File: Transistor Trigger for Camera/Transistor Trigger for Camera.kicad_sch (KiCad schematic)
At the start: 10 parts, among them J1 Conn_01x01_Pin, J2 Conn_01x01_Pin, J3 Conn_01x01_Pin, J4 Conn_01x01_Pin, J5 Conn_01x01_Pin, J6 Conn_01x01_Pin, Q1 2N4401, U1 74HC14N_652

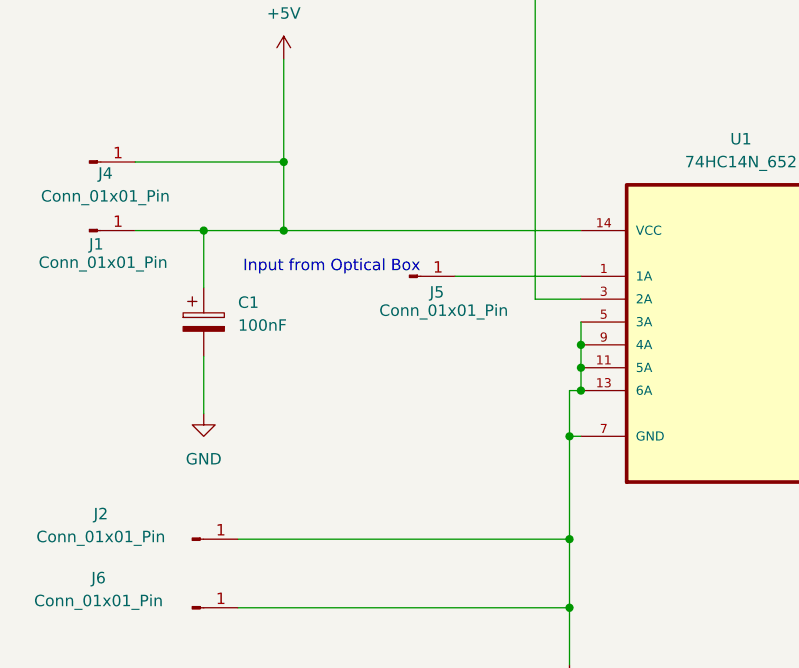
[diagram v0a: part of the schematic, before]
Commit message: second update with new 100k resistor
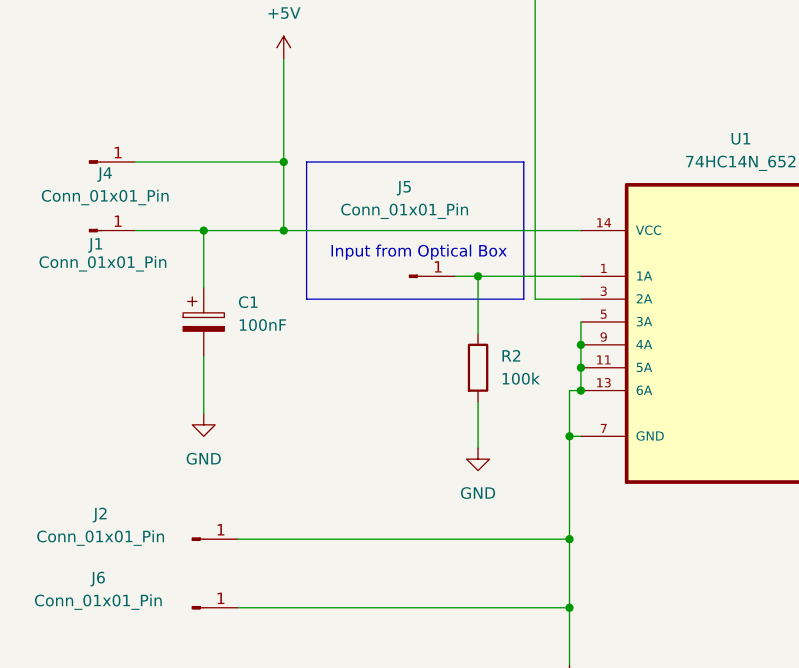
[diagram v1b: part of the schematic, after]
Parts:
- added R2: 100k, Resistor_THT:R_Axial_DIN0207_L6.3mm_D2.5mm_P15.24mm_Horizontal, symbol Device:R
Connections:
- net GND: now also R2.2
- net at J5.1 (Pin_1), U1.1 (1A): now also R2.1
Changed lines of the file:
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@@
+	)
+	(junction
+		(at 63.5 91.44)
+		(diameter 0)
+		(color 0 0 0 0)
 	)
 	(junction
@@
 	(wire
 		(pts
+			(xy 63.5 105.41) (xy 63.5 110.49)
+		)
+		(stroke
+			(width 0)
+			(type default)
+		)
+	)
+	(wire
+		(pts
 			(xy 113.03 57.15) (xy 69.85 57.15)
 		)
@@
 	(wire
 		(pts
+			(xy 63.5 91.44) (xy 63.5 97.79)
+		)
+		(stroke
+			(width 0)
+			(type default)
+		)
+	)
+	(wire
+		(pts
 			(xy 25.4 78.74) (xy 41.91 78.74)
 		)
@@
 	(wire
 		(pts
-			(xy 60.96 91.44) (xy 74.93 91.44)
+			(xy 60.96 91.44) (xy 63.5 91.44)
 		)
 		(stroke
@@
 		(pts
 			(xy 110.49 88.9) (xy 146.05 88.9)
+		)
+		(stroke
+			(width 0)
+			(type default)
+		)
+	)
+	(wire
+		(pts
+			(xy 63.5 91.44) (xy 74.93 91.44)
 		)
 		(stroke
@@
 		)
 	)
+	(rectangle
+		(start 44.45 78.74)
+		(end 68.58 93.98)
+		(stroke
+			(width 0)
+			(type default)
+		)
+		(fill
+			(type none)
+		)
+	)
 	(text "Input from Optical Box"
 		(exclude_from_sim no)
-		(at 47.244 90.424 0)
+		(at 56.896 88.9 0)
 		(effects
 			(font
@@
 	)
 	(symbol
+		(lib_id "Device:R")
+		(at 63.5 101.6 0)
+		(unit 1)
+		(exclude_from_sim no)
+		(in_bom yes)
+		(on_board yes)
+		(dnp no)
+		(fields_autoplaced yes)
+		(property "Reference" "R2"
+			(at 66.04 100.3299 0)
+			(effects
+				(font
+					(size 1.27 1.27)
+				)
+				(justify left)
+			)
+		)
+		(property "Value" "100k"
+			(at 66.04 102.8699 0)
+			(effects
+				(font
+					(size 1.27 1.27)
+				)
+				(justify left)
+			)
+		)
+		(property "Footprint" "Resistor_THT:R_Axial_DIN0207_L6.3mm_D2.5mm_P15.24mm_Horizontal"
+			(at 61.722 101.6 90)
+			(effects
+				(font
+					(size 1.27 1.27)
+				)
+				(hide yes)
+			)
+		)
+		(property "Datasheet" "~"
+			(at 63.5 101.6 0)
+			(effects
+				(font
+					(size 1.27 1.27)
+				)
+				(hide yes)
+			)
+		)
+		(property "Description" "Resistor"
+			(at 63.5 101.6 0)
+			(effects
+				(font
+					(size 1.27 1.27)
+				)
+				(hide yes)
+			)
+		)
+		(property "Purpose" ""
+			(at 63.5 101.6 0)
+			(effects
+				(font
+					(size 1.27 1.27)
+				)
+				(hide yes)
+			)
+		)
+		(pin "1"
+		)
+		(pin "2"
+		)
+		(instances
+			(project "Transistor Trigger for Camera"
+				(path "/dd946c7e-f666-4bcd-b1d4-6ed21bf15a43"
+					(reference "R2")
+					(unit 1)
+				)
+			)
+		)
+	)
+	(symbol
+		(lib_id "power:GND")
+		(at 63.5 110.49 0)
+		(unit 1)
+		(exclude_from_sim no)
+		(in_bom yes)
+		(on_board yes)
+		(dnp no)
+		(fields_autoplaced yes)
+		(property "Reference" "#PWR07"
+			(at 63.5 116.84 0)
+			(effects
+				(font
+					(size 1.27 1.27)
+				)
+				(hide yes)
+			)
+		)
+		(property "Value" "GND"
+			(at 63.5 115.57 0)
+			(effects
+				(font
+					(size 1.27 1.27)
+				)
+			)
+		)
+		(property "Footprint" ""
+			(at 63.5 110.49 0)
+			(effects
+				(font
+					(size 1.27 1.27)
+				)
+				(hide yes)
+			)
+		)
+		(property "Datasheet" ""
+			(at 63.5 110.49 0)
+			(effects
+				(font
+					(size 1.27 1.27)
+				)
+				(hide yes)
+			)
+		)
+		(property "Description" "Power symbol creates a global label with name \"GND\" , ground"
+			(at 63.5 110.49 0)
+			(effects
+				(font
+					(size 1.27 1.27)
+				)
+				(hide yes)
+			)
+		)
+		(pin "1"
+		)
+		(instances
+			(project "Transistor Trigger for Camera"
+				(path "/dd946c7e-f666-4bcd-b1d4-6ed21bf15a43"
+					(reference "#PWR07")
+					(unit 1)
+				)
+			)
+		)
+	)
+	(symbol
 		(lib_id "Connector:Conn_01x01_Pin")
 		(at 55.88 91.44 0)
@@
 		(dnp no)
 		(property "Reference" "J5"
-			(at 58.928 93.218 0)
+			(at 55.372 81.534 0)
 			(effects
 				(font
@@
 		)
 		(property "Value" "Conn_01x01_Pin"
-			(at 59.69 95.25 0)
-			(effects
-				(font
+			(at 55.372 84.074 0)
+			(effects
+				(font

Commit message: third update with Mark and parts
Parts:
- removed C1: 100nF, Capacitor_THT:CP_Radial_D8.0mm_P5.00mm, symbol Device:C_Polarized
- added C1: 100nF, Capacitor_THT:CP_Radial_D8.0mm_P5.00mm, symbol Device:C
- R1: value R -> 10
- R2: value 100k -> 22k
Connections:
- net +5V: now also C1.1
- net GND: now also C1.2
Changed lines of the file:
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@@
+	)
+	(symbol
+		(lib_id "Device:C")
+		(at 33.02 96.52 0)
+		(unit 1)
+		(exclude_from_sim no)
+		(in_bom yes)
+		(on_board yes)
+		(dnp no)
+		(fields_autoplaced yes)
+		(property "Reference" "C1"
+			(at 36.83 95.2499 0)
+			(effects
+				(font
+					(size 1.27 1.27)
+				)
+				(justify left)
+			)
+		)
+		(property "Value" "100nF"
+			(at 36.83 97.7899 0)
+			(effects
+				(font
+					(size 1.27 1.27)
+				)
+				(justify left)
+			)
+		)
+		(property "Footprint" "Capacitor_THT:CP_Radial_D8.0mm_P5.00mm"
+			(at 33.9852 100.33 0)
+			(effects
+				(font
+					(size 1.27 1.27)
+				)
+				(hide yes)
+			)
+		)
+		(property "Datasheet" "~"
+			(at 33.02 96.52 0)
+			(effects
+				(font
+					(size 1.27 1.27)
+				)
+				(hide yes)
+			)
+		)
+		(property "Description" "Unpolarized capacitor"
+			(at 33.02 96.52 0)
+			(effects
+				(font
+					(size 1.27 1.27)
+				)
+				(hide yes)
+			)
+		)
+		(property "Purpose" ""
+			(at 33.02 96.52 0)
+			(effects
+				(font
+					(size 1.27 1.27)
+				)
+				(hide yes)
+			)
+		)
+		(pin "1"
+		)
+		(pin "2"
+		)
+		(instances
+			(project ""
+				(path "/dd946c7e-f666-4bcd-b1d4-6ed21bf15a43"
+					(reference "C1")
+					(unit 1)
+				)
+			)
+		)
 	)
 	(symbol
@@
 			)
 		)
-		(property "Value" "100k"
+		(property "Value" "22k"
 			(at 66.04 102.8699 0)
 			(effects
@@
 			)
 		)
-		(property "Value" "R"
+		(property "Value" "10"
 			(at 153.67 73.6599 0)
 			(effects
@@
 		)
 		(property "Description" "Resistor"
+			(at 151.13 72.39 0)
+			(effects
+				(font
+					(size 1.27 1.27)
+				)
+				(hide yes)
+			)
+		)
+		(property "Purpose" ""
 			(at 151.13 72.39 0)
 			(effects
@@
 					(unit 1)
 				)
-			)
-		)
-	)
-	(symbol
-		(lib_id "Device:C_Polarized")
-		(at 33.02 96.52 0)
-		(unit 1)
-		(exclude_from_sim no)
-		(in_bom yes)
-		(on_board yes)
-		(dnp no)
-		(fields_autoplaced yes)
-		(property "Reference" "C1"
-			(at 36.83 94.3609 0)
-			(effects
-				(font
-					(size 1.27 1.27)
-				)
-				(justify left)
-			)
-		)
-		(property "Value" "100nF"
-			(at 36.83 96.9009 0)
-			(effects
-				(font
-					(size 1.27 1.27)
-				)
-				(justify left)
-			)
-		)
-		(property "Footprint" "Capacitor_THT:CP_Radial_D8.0mm_P5.00mm"
-			(at 33.9852 100.33 0)
-			(effects
-				(font
-					(size 1.27 1.27)
-				)
-				(hide yes)
-			)
-		)
-		(property "Datasheet" "~"
-			(at 33.02 96.52 0)
-			(effects
-				(font
-					(size 1.27 1.27)
-				)
-				(hide yes)
-			)
-		)
-		(property "Description" "Polarized capacitor"
-			(at 33.02 96.52 0)
-			(effects
-				(font
-					(size 1.27 1.27)
-				)
-				(hide yes)
-			)
-		)
-		(property "Purpose" ""
-			(at 33.02 96.52 0)
-			(effects
-				(font
-					(size 1.27 1.27)
-				)
-				(hide yes)
-			)
-		)
-		(pin "2"
-		)
-		(pin "1"
-		)
-		(instances
-			(project ""
-				(path "/dd946c7e-f666-4bcd-b1d4-6ed21bf15a43"
-					(reference "C1")
-					(unit 1)
-				)

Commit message: Final revistion changes for layout
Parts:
- added D1: D, Diode_THT:D_T-1_P10.16mm_Horizontal, symbol Device:D
- added D2: D_Zener, Diode_THT:D_T-1_P10.16mm_Horizontal, symbol Device:D_Zener
- R2: value 22k -> 10k
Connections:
- net GND: now also D2.2 (A)
- net at J3.1 (Pin_1), Q1.1: now also D1.2 (A), D2.1 (K)
- net at Q1.2, U1.4 (2Y): now also D1.1 (K)
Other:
- note added: "4148 type"
- note added: "5v type"
